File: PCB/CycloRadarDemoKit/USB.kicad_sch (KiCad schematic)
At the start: 19 parts, among them J301 USB_C_Receptacle_USB2.0, Q301 L8050QLT1G, Q302 L8050QLT1G, U301 CP2102N-Axx-xQFN24

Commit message: reanotated schematic, routing started
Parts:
- renumbered C302 to C601, C301 to C602, D301 to D601, D302 to D602, D303 to D603, FB301 to FB601, J301 to J601, Q301 to Q601, Q302 to Q602, R301 to R601, R302 to R602, R303 to R603, R304 to R604, R305 to R605, R306 to R606, R307 to R607, R308 to R608, R309 to R609, U301 to U601

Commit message: Parts ordered on PCB, 1206->0803 10uF, 0803->0402 1uF
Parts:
- C601, C602: value 1uF/50V(10%) -> 1uF/25V(10%); footprint Capacitor_SMD:C_0603_1608Metric -> Capacitor_SMD:C_0402_1005Metric; LCSC C15849 -> C52923
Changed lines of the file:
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@@
       (effects (font (size 1.27 1.27)) (justify left))
     )
-    (property "Value" "1uF/50V(10%)" (at 189.23 76.2063 0)
-      (effects (font (size 1.27 1.27)) (justify left))
-    )
-    (property "Footprint" "Capacitor_SMD:C_0603_1608Metric" (at 186.69 74.93 0)
+    (property "Value" "1uF/25V(10%)" (at 189.23 76.2063 0)
+      (effects (font (size 1.27 1.27)) (justify left))
+    )
+    (property "Footprint" "Capacitor_SMD:C_0402_1005Metric" (at 186.69 74.93 0)
       (effects (font (size 1.27 1.27)) hide)
     )
@@
       (effects (font (size 1.27 1.27)) hide)
     )
-    (property "LCSC" "C15849" (at 186.69 74.93 0)
+    (property "LCSC" "C52923" (at 186.69 74.93 0)
       (effects (font (size 1.27 1.27)) hide)
     )
@@
       (effects (font (size 1.27 1.27)))
     )
-    (property "Value" "1uF/50V(10%)" (at 176.5363 72.39 90)
-      (effects (font (size 1.27 1.27)))
-    )
-    (property "Footprint" "Capacitor_SMD:C_0603_1608Metric" (at 176.53 76.2 0)
+    (property "Value" "1uF/25V(10%)" (at 176.5363 72.39 90)
+      (effects (font (size 1.27 1.27)))
+    )
+    (property "Footprint" "Capacitor_SMD:C_0402_1005Metric" (at 176.53 76.2 0)
       (effects (font (size 1.27 1.27)) hide)
     )
@@
       (effects (font (size 1.27 1.27)) hide)
     )
-    (property "LCSC" "C15849" (at 176.53 76.2 0)
-      (effects (font (size 1.27 1.27)) hide)
-    )
+    (property "LCSC" "C52923" (at 176.53 76.2 0)
+      (effects (font (size 1.27 1.27)) hide)
+    )

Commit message: USB layout, long traces from upper prepaired
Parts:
- J601: footprint Connector_USB:USB_C_Receptacle_GCT_USB4110 -> Connector_USB:TYPE-C-SMD_YIYUAN_YTC-TC16-273A1
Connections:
- net DP: now reaches D603.4 (K), J601.A6 (D+), J601.B6 (D+), U601.3 (D+)
- net DN: now reaches D603.3 (K), J601.A7 (D-), J601.B7 (D-), U601.4 (D-)

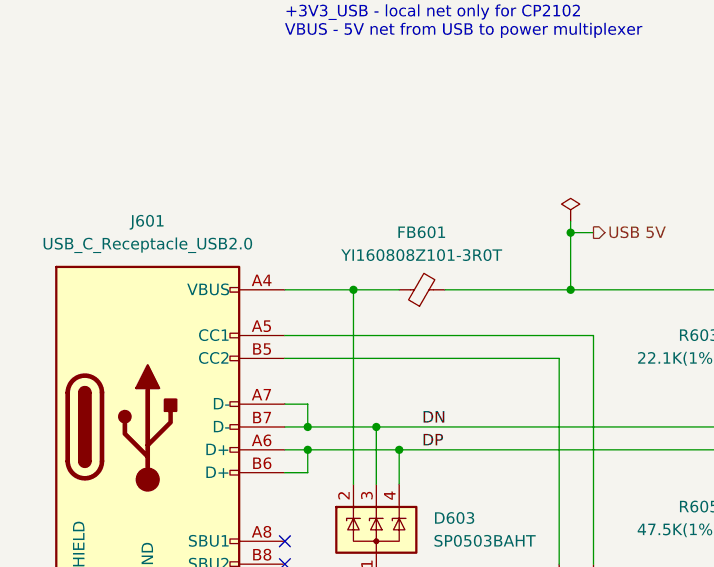
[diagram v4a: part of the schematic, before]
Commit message: DC/DC placement, conn-s swaped
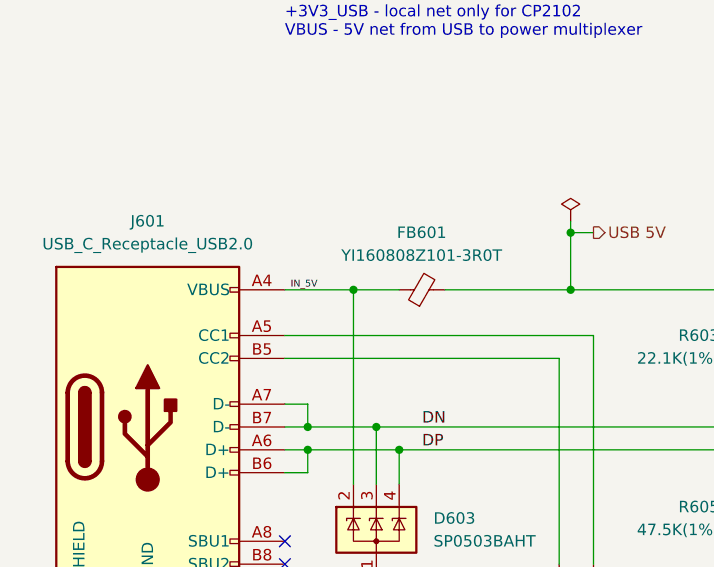
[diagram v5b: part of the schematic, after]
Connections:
- net IN_5V: now reaches D603.2 (K), FB601.1, J601.A4 (VBUS), J601.A9 (VBUS), J601.B4 (VBUS), J601.B9 (VBUS)
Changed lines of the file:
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@@
     (effects (font (size 1.27 1.27)) (justify left bottom))
+  )
+  (label "IN_5V" (at 85.725 86.36 0) (fields_autoplaced)
+    (effects (font (size 0.762 0.762)) (justify left bottom))
   )
   (label "DP" (at 100.33 104.14 0) (fields_autoplaced)

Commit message: start of repair after review
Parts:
- U601: LCSC C964632 -> C969151
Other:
- note added: "https://datasheet.lcsc.com/lcsc/2108132230_TECH-PUBLIC-USBLC6-2SC6_C2827654.pdf"
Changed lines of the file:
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@@
+    (effects (font (size 1.27 1.27)) (justify left bottom))
+  )
+  (text "https://datasheet.lcsc.com/lcsc/2108132230_TECH-PUBLIC-USBLC6-2SC6_C2827654.pdf"
+    (at 40.64 139.7 0)
     (effects (font (size 1.27 1.27)) (justify left bottom))
   )
@@
       (effects (font (size 1.27 1.27)) hide)
     )
-    (property "LCSC" "C964632" (at 157.48 109.22 0)
-      (effects (font (size 1.27 1.27)) hide)
-    )
+    (property "LCSC" "C969151" (at 157.48 109.22 0)
+      (effects (font (size 1.27 1.27)) hide)
+    )

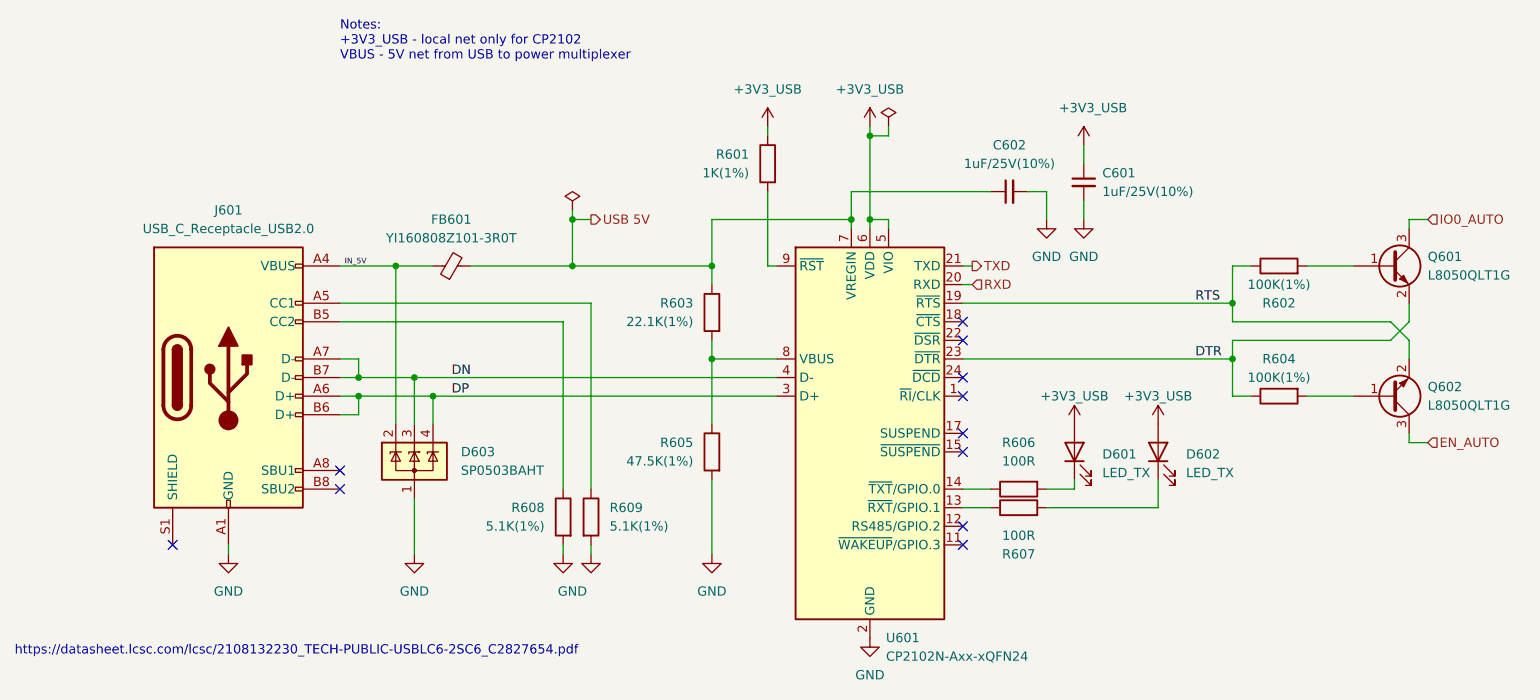
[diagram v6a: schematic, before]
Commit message: Review changes WIP, USB ESD changed, MDIC pullup added
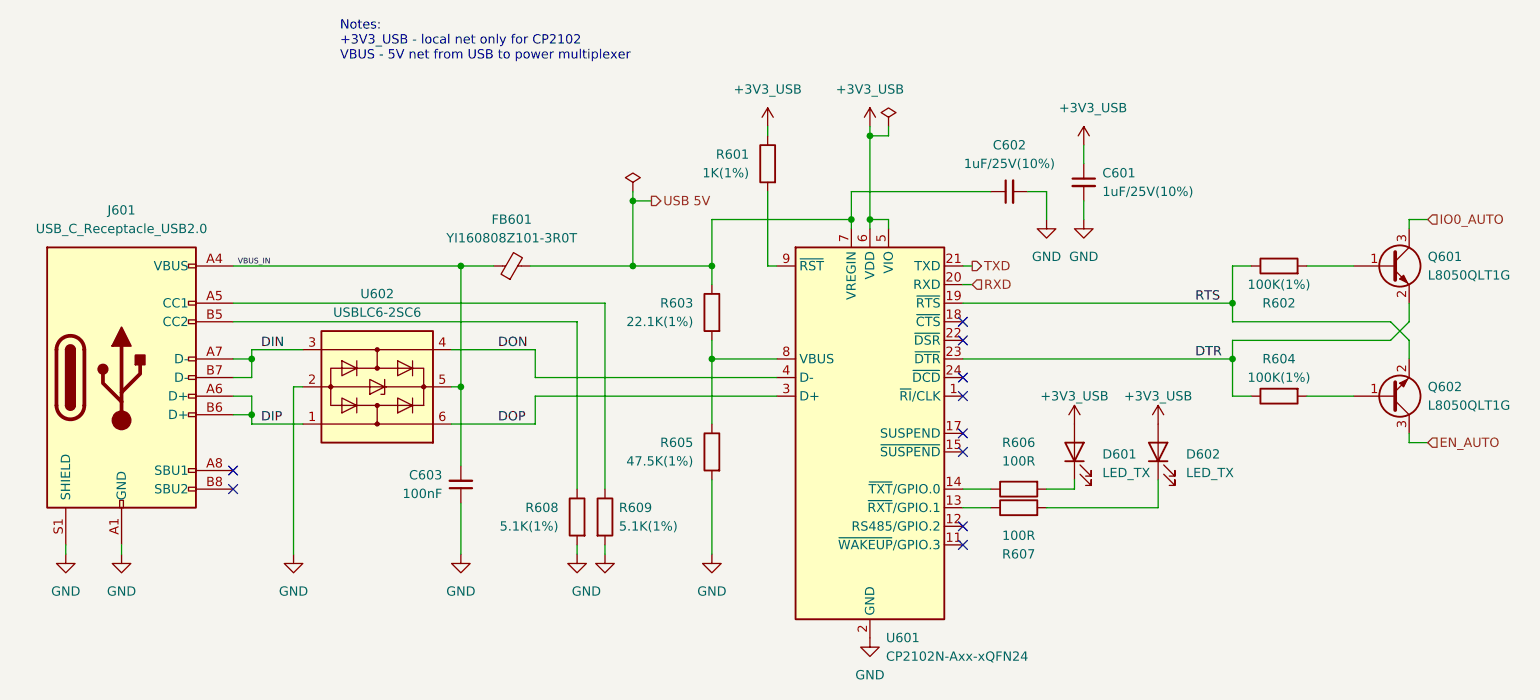
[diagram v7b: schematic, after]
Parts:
- removed D603: SP0503BAHT, Package_TO_SOT_SMD:SOT-143, symbol Power_Protection:SP0503BAHT
- added C603: 100nF, Capacitor_SMD:C_0402_1005Metric, symbol Device:C_Small
- added U602: USBLC6-2SC6, Package_TO_SOT_SMD:SOT-23-6, symbol Power_Protection:USBLC6-2SC6
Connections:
- net GND: now also J601.S1 (SHIELD), C603.1, U602.2 (GND)
- net DN renamed DIN
- net DIN: now also U602.3 (I/O2); no longer U601.4 (D-)
- net DP renamed DIP
- net DIP: now also U602.1 (I/O1); no longer U601.3 (D+)
- net IN_5V renamed VBUS_IN
- net VBUS_IN: now also C603.2, U602.5 (VBUS)
- new net DON: U601.4 (D-), U602.4 (I/O2)
- new net DOP: U601.3 (D+), U602.6 (I/O1)
- no-connect marks 11 -> 10
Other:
- note removed: "https://datasheet.lcsc.com/lcsc/2108132230_TECH-PUBLIC-USBLC6-2SC6_C2827654.pdf"
- moved on the sheet: FB601, J601, R608, R609

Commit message: PCB finished and reviewed
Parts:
- C603: LCSC C52923 -> (none)
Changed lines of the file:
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@@
       (effects (font (size 1.27 1.27)) hide)
     )
-    (property "LCSC" "C52923" (at 101.6 116.205 0)
+    (property "LCSC" "" (at 101.6 116.205 0)
       (effects (font (size 1.27 1.27)) hide)
     )
